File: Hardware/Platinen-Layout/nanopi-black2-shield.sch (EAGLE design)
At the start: 8 parts, among them IC2 LM3940IT-3.3

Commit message: new hardware + test code
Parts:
- added J3: (no value), 61300211821_Eagle_WR-PHD_rev19a:6130XX11121_61300211121
- added R4, R5: 2.2k, SparkFun-Resistors:2.2KOHM-0603-1/10W-1%
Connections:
- net 3.3V: now also R4.2, R5.2
- net 5V-1: now also J3.2
- net GND: now also J3.1
- net I2C_SCL0: now also R5.1
- net I2C_SDA0: now also R4.1
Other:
- note added: "External 5V"
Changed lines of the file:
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@@
 <part name="GND4" library="supply1" library_urn="urn:adsk.eagle:library:371" deviceset="GND" device=""/>
 <part name="GND5" library="supply1" library_urn="urn:adsk.eagle:library:371" deviceset="GND" device=""/>
+<part name="J3" library="61300211821_Eagle_WR-PHD_rev19a" deviceset="6130XX11121_61300211121" device="" package3d_urn="urn:adsk.eagle:package:14805431/3"/>
+<part name="GND2" library="supply1" library_urn="urn:adsk.eagle:library:371" deviceset="GND" device=""/>
+<part name="SUPPLY15" library="SparkFun-PowerSymbols" deviceset="3.3V" device=""/>
+<part name="SUPPLY16" library="SparkFun-PowerSymbols" deviceset="3.3V" device=""/>
+<part name="R4" library="SparkFun-Resistors" deviceset="2.2KOHM" device="-0603-1/10W-1%" value="2.2k"/>
+<part name="R5" library="SparkFun-Resistors" deviceset="2.2KOHM" device="-0603-1/10W-1%" value="2.2k"/>
 </parts>
 <sheets>
@@
 <text x="96.52" y="68.58" size="1.778" layer="97">GPIO Pionout</text>
 <text x="93.98" y="43.18" size="1.778" layer="125">Status LED's</text>
+<text x="193.04" y="68.58" size="1.778" layer="95">External 5V</text>
 </plain>
 <instances>
@@
 <instance part="GND5" gate="1" x="106.68" y="17.78" smashed="yes">
 <attribute name="VALUE" x="104.14" y="15.24" size="1.778" layer="96"/>
+</instance>
+<instance part="J3" gate="G$1" x="193.04" y="60.96" smashed="yes" rot="R90">
+<attribute name="NAME" x="194.245" y="55.97" size="1.016" layer="95" rot="R90" align="bottom-right"/>
+<attribute name="VALUE" x="196.05" y="56.01" size="1.016" layer="96" rot="R90" align="bottom-right"/>
+</instance>
+<instance part="GND2" gate="1" x="198.12" y="53.34" smashed="yes">
+<attribute name="VALUE" x="195.58" y="50.8" size="1.778" layer="96"/>
+</instance>
+<instance part="SUPPLY15" gate="G$1" x="200.66" y="17.78" smashed="yes">
+<attribute name="VALUE" x="200.66" y="20.574" size="1.778" layer="96" align="bottom-center"/>
+</instance>
+<instance part="SUPPLY16" gate="G$1" x="220.98" y="17.78" smashed="yes">
+<attribute name="VALUE" x="220.98" y="20.574" size="1.778" layer="96" align="bottom-center"/>
+</instance>
+<instance part="R4" gate="G$1" x="220.98" y="10.16" smashed="yes" rot="R90">
+<attribute name="NAME" x="219.456" y="10.16" size="1.778" layer="95" font="vector" rot="R90" align="bottom-center"/>
+<attribute name="VALUE" x="222.504" y="10.16" size="1.778" layer="96" font="vector" rot="R90" align="top-center"/>
+</instance>
+<instance part="R5" gate="G$1" x="200.66" y="10.16" smashed="yes" rot="R90">
+<attribute name="NAME" x="199.136" y="10.16" size="1.778" layer="95" font="vector" rot="R90" align="bottom-center"/>
+<attribute name="VALUE" x="202.184" y="10.16" size="1.778" layer="96" font="vector" rot="R90" align="top-center"/>
 </instance>
 </instances>
@@
 <wire x1="93.98" y1="20.32" x2="93.98" y2="22.86" width="0.1524" layer="91"/>
 </segment>
+<segment>
+<pinref part="GND2" gate="1" pin="GND"/>
+<pinref part="J3" gate="G$1" pin="1"/>
+<wire x1="198.12" y1="55.88" x2="198.12" y2="58.42" width="0.1524" layer="91"/>
+</segment>
 </net>
 <net name="5V-1" class="0">
@@
 <junction x="144.78" y="60.96"/>
 </segment>
+<segment>
+<label x="203.2" y="60.96" size="1.27" layer="95" xref="yes"/>
+<pinref part="J3" gate="G$1" pin="2"/>
+<wire x1="198.12" y1="60.96" x2="203.2" y2="60.96" width="0.1524" layer="91"/>
+</segment>
 </net>
 <net name="GPIOA2" class="0">
@@
 <label x="152.4" y="12.7" size="1.778" layer="95" xref="yes"/>
 </segment>
+<segment>
+<wire x1="200.66" y1="5.08" x2="200.66" y2="2.54" width="0.1524" layer="91"/>
+<wire x1="198.12" y1="2.54" x2="200.66" y2="2.54" width="0.1524" layer="91"/>
+<label x="198.12" y="2.54" size="1.27" layer="95" rot="R180" xref="yes"/>
+<pinref part="R5" gate="G$1" pin="1"/>
+</segment>
 </net>
 <net name="I2C_SDA0" class="0">
@@
 <wire x1="149.86" y1="20.32" x2="152.4" y2="20.32" width="0.1524" layer="91"/>
 <label x="152.4" y="20.32" size="1.778" layer="95" xref="yes"/>
+</segment>
+<segment>
+<wire x1="220.98" y1="5.08" x2="220.98" y2="2.54" width="0.1524" layer="91"/>
+<wire x1="220.98" y1="2.54" x2="218.44" y2="2.54" width="0.1524" layer="91"/>
+<label x="218.44" y="2.54" size="1.27" layer="95" rot="R180" xref="yes"/>
+<pinref part="R4" gate="G$1" pin="1"/>
 </segment>
 </net>
@@
 <pinref part="C2" gate="G$1" pin="1"/>
 </segment>
-</net>
+<segment>
+<wire x1="200.66" y1="15.24" x2="200.66" y2="17.78" width="0.1524" layer="91"/>
+<pinref part="SUPPLY15" gate="G$1" pin="3.3V"/>
+<pinref part="R5" gate="G$1" pin="2"/>
+</segment>
+<segment>
+<pinref part="SUPPLY16" gate="G$1" pin="3.3V"/>
+<wire x1="220.98" y1="17.78" x2="220.98" y2="15.24" width="0.1524" layer="91"/>
+<pinref part="R4" gate="G$1" pin="2"/>
+</segment>
+</net>

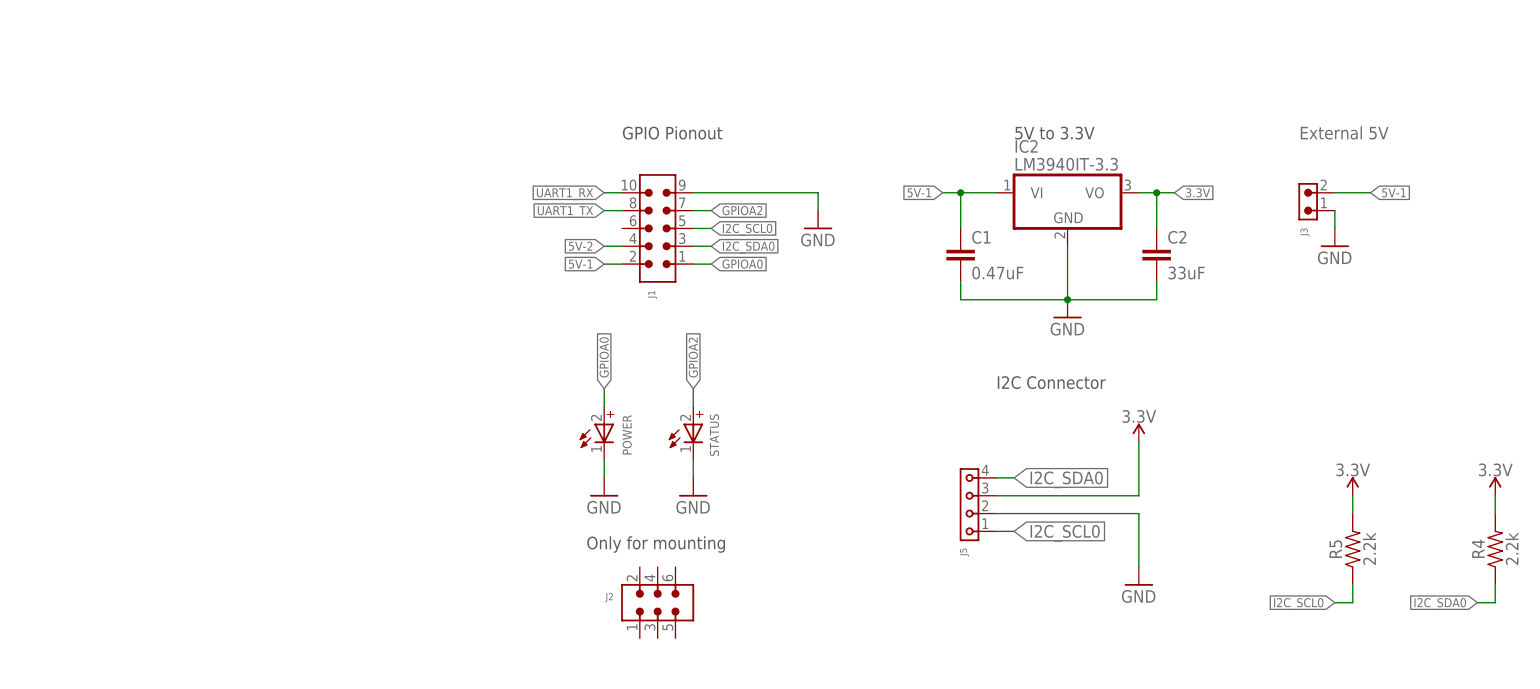
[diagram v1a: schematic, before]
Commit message: new adapter Board
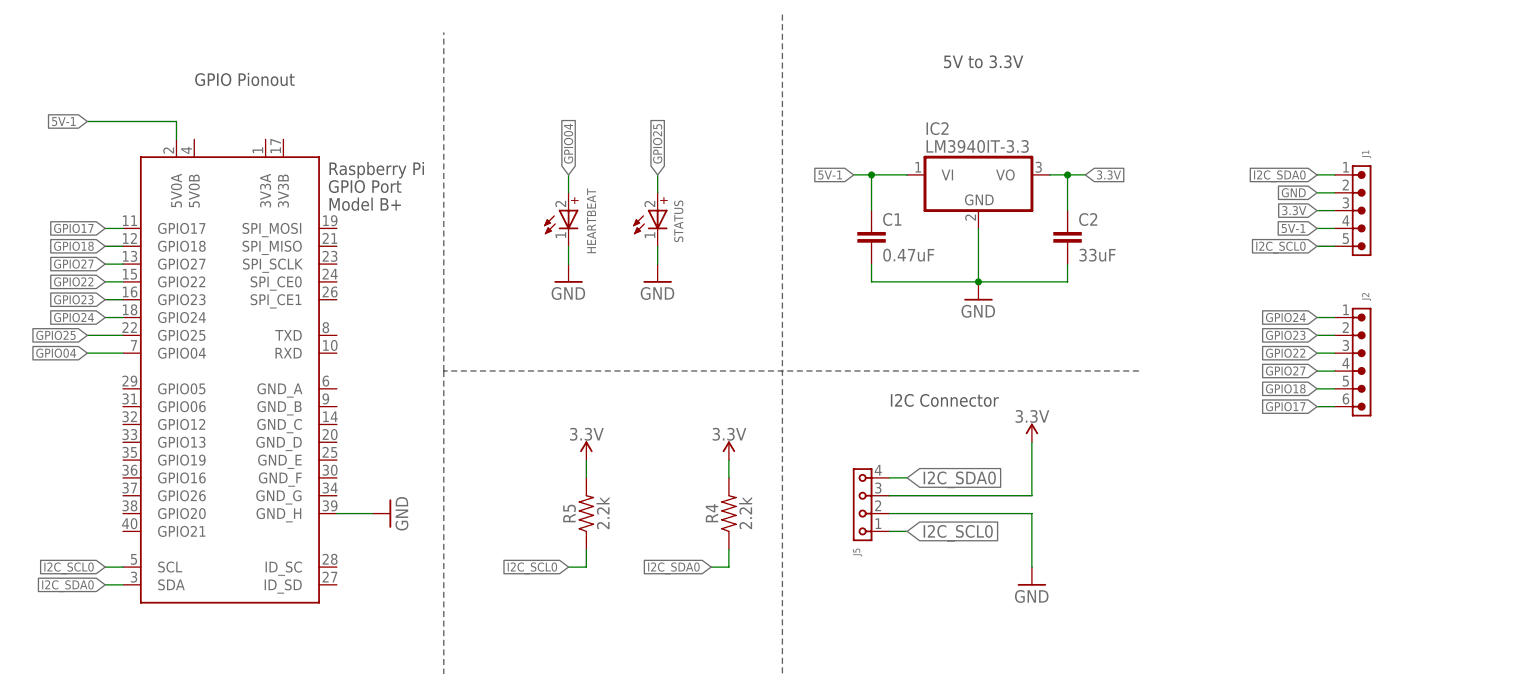
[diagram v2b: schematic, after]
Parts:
- removed J3: (no value), 61300211821_Eagle_WR-PHD_rev19a:6130XX11121_61300211121
- removed POWER: (no value), 155060GS75300_Eagle_WL-SMSW_rev20b:WL-SMSW_0603_REC_155060RS75300
- added HEARTBEAT: (no value), 155060GS75300_Eagle_WL-SMSW_rev20b:WL-SMSW_0603_REC_155060RS75300
- added X1: RASPI_BOARD_B+#_HDC, raspberrypi_bastelstube_v13:RASPI_BOARD_B+#_HDC
- J1: device 61300211821_Eagle_WR-PHD_rev19a:6130XX21121_61301021121 -> 61300621821_Eagle_WR-PHD_rev19a:6130XX11121_61300511121
- J2: device 61300211821_Eagle_WR-PHD_rev19a:6130XX21121_61300621121 -> 61300621821_Eagle_WR-PHD_rev19a:6130XX11121_61300611121
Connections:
- removed net 5V-2: J1.4
- removed net GPIOA0: J1.1, POWER.+
- removed net GPIOA2: J1.7, STATUS.+
- removed net UART1_RX: J1.10
- removed net UART1_TX: J1.8
- new net GPIO04: HEARTBEAT.+, X1.GPIO04
- new net GPIO17: J2.6, X1.GPIO17
- new net GPIO18: J2.5, X1.GPIO18
- new net GPIO22: J2.3, X1.GPIO22
- new net GPIO23: J2.2, X1.GPIO23
- new net GPIO24: J2.1, X1.GPIO24
- new net GPIO25: STATUS.+, X1.GPIO25
- new net GPIO27: J2.4, X1.GPIO27
- net 3.3V: now also J1.3
- net 5V-1: now also J1.4, X1.5V0A; no longer J1.2, J3.2
- net GND: now also HEARTBEAT.-, J1.2, X1.GND_H; no longer J1.9, J3.1, POWER.-
- net I2C_SCL0: now also X1.SCL
- net I2C_SDA0: now also J1.1, X1.SDA; no longer J1.3
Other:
- note added: "Pull Up"
- note removed: "External 5V"
- note removed: "Only for mounting"
- moved on the sheet: C1, C2, IC2, J5, R4, R5, STATUS
